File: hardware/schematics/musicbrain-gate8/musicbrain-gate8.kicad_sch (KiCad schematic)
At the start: 15 parts, among them J1 BUS, J2 GATES OUT, U1 74HCT595, U2 AMS1117-5.0

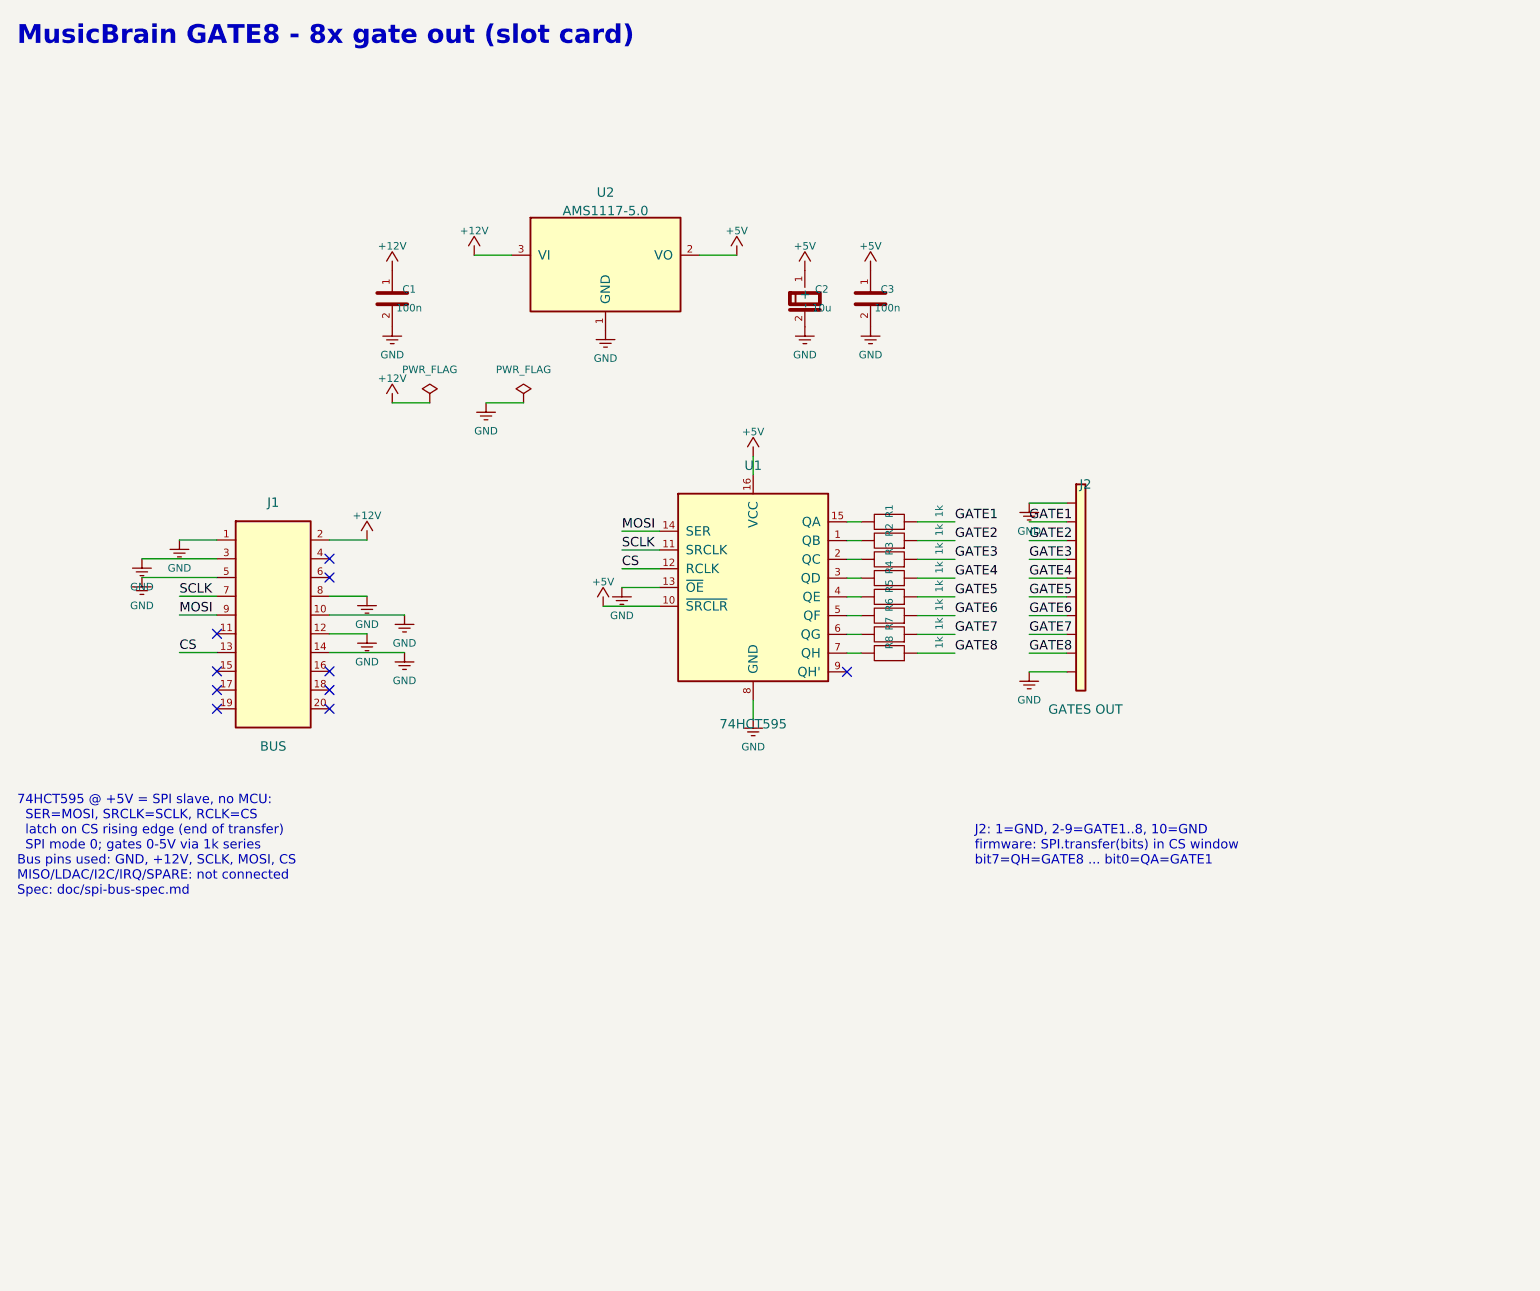
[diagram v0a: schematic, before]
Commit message: gate8 gen 2: 80x45, slot 2x12, freerouting; generator naar cardlib
- gen_gate.py (schlib+cardlib) vervangt gen_gate_sch.py + gen_gate_pcb_v11.py
  (gen 1, 35x80, eigen sexpr-bouwer van voor cardlib)
- J1 2x10 -> 2x12 via bus.j1_map; J2 1x10 gecentreerd, paneelinzet 4,04
- U1 74HCT595 rot 270: Q-uitgangen noord naar de 1k-kolommen, SPI/GND zuid
- AMS1117-5.0 + ontkoppeling in de oosthelft; +5V blijft lokaal
- prep_dsn.py: DSN-prep (GND-strip + randkrimp) nu een repo-script
- ERC 0, netcheck OK, DRC 0/0

Co-Authored-By: Claude Fable 5 <noreply@anthropic.com>
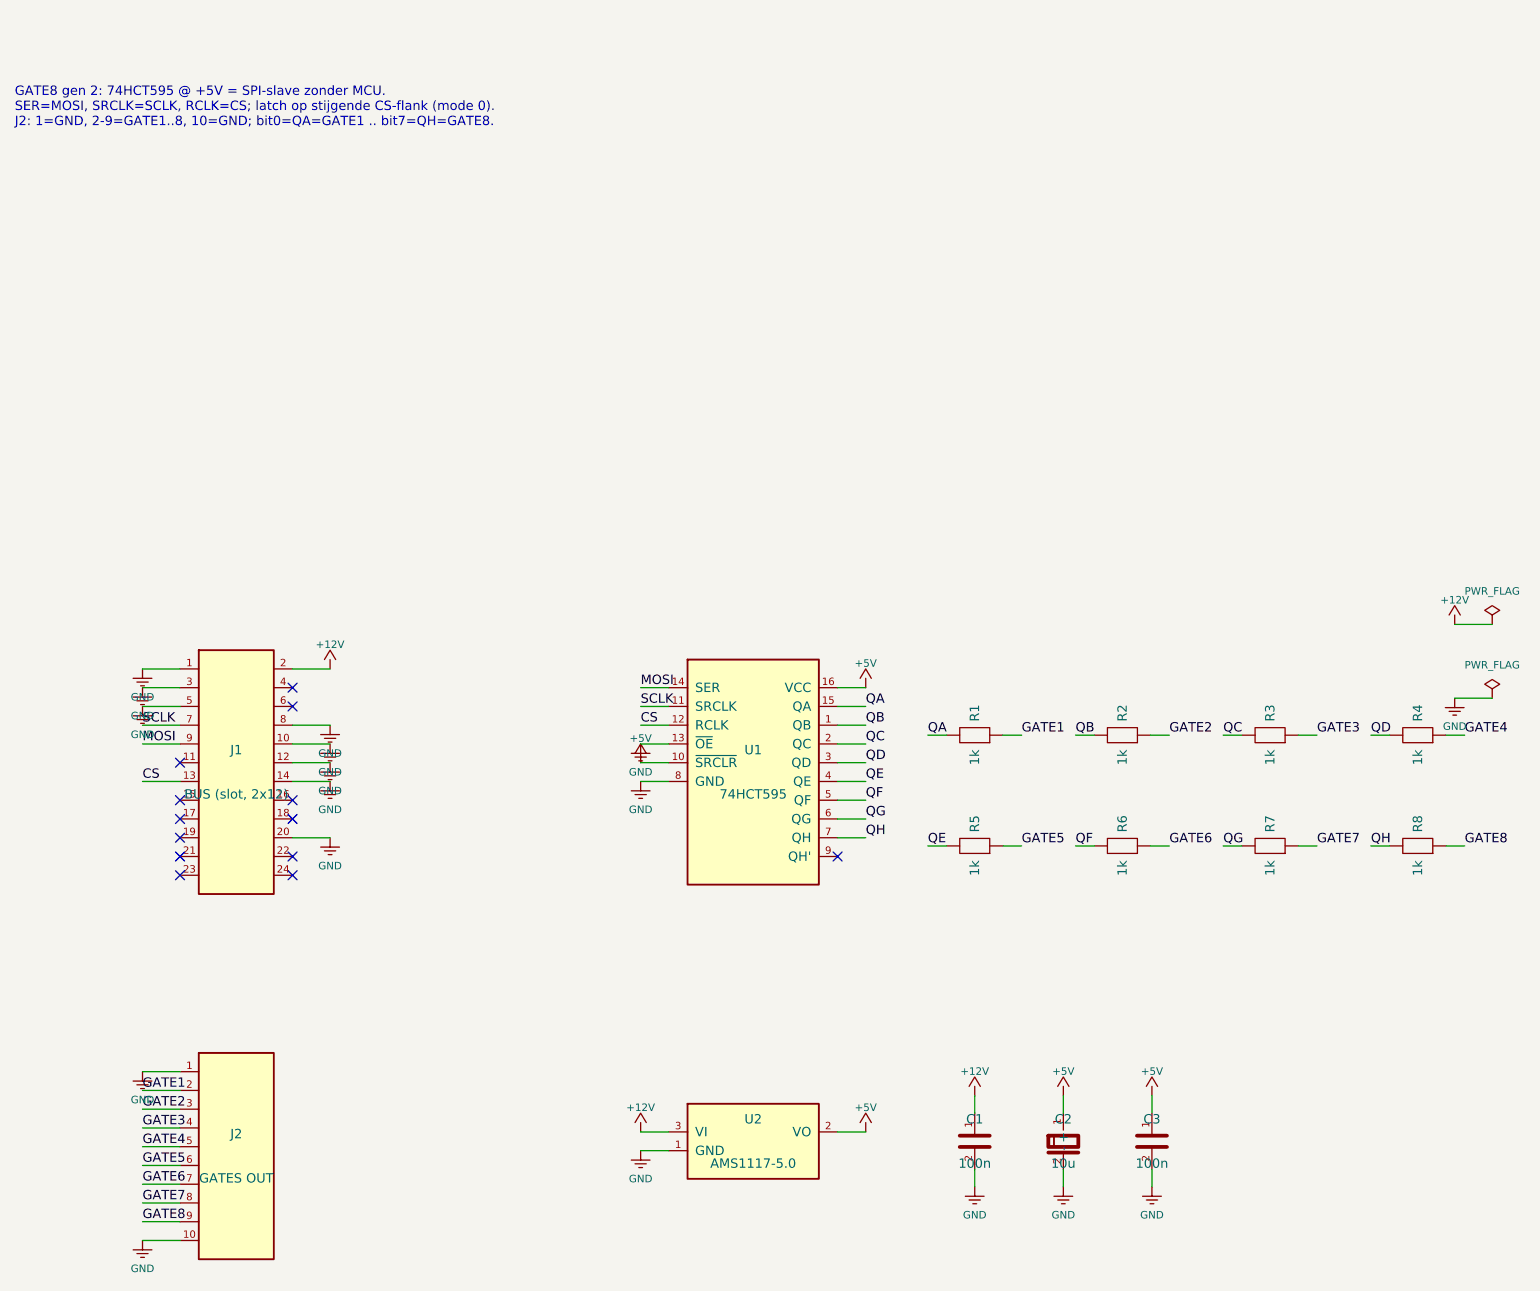
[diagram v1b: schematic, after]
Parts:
- removed J1: BUS, Connector_PinHeader_2.54mm:PinHeader_2x10_P2.54mm_Horizontal, symbol Custom:Conn_02x10
- added J1: BUS (slot, 2x12), Connector_PinHeader_2.54mm:PinHeader_2x12_P2.54mm_Horizontal, symbol Custom:Conn_02x12
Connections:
- net +12V: now also J1.2 (Pin_2)
- net CS: now also J1.13 (Pin_13)
- net GND: now also J1.1 (Pin_1), J1.10 (Pin_10), J1.12 (Pin_12), J1.14 (Pin_14), J1.20 (Pin_20), J1.3 (Pin_3), J1.5 (Pin_5), J1.8 (Pin_8)
- net MOSI: now also J1.9 (Pin_9)
- net SCLK: now also J1.7 (Pin_7)
- net QB: now reaches R2.1, U1.1 (QB)
- net QA: now reaches R1.1, U1.15 (QA)
- net QC: now reaches R3.1, U1.2 (QC)
- net QD: now reaches R4.1, U1.3 (QD)
- net QE: now reaches R5.1, U1.4 (QE)
- net QF: now reaches R6.1, U1.5 (QF)
- net QG: now reaches R7.1, U1.6 (QG)
- net QH: now reaches R8.1, U1.7 (QH)
- no-connect marks 10 -> 13
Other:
- note added: "GATE8 gen 2: 74HCT595 @ +5V = SPI-slave zonder MCU. SER=MOSI, SRCLK=SCLK, RCLK=CS; latch op stijgende CS-flank (mode 0). J2: 1=GND, 2-9=GATE1..8, 10=GND; bit0=QA=GATE1 .. bit7=QH=GATE8."
- note removed: "74HCT595 @ +5V = SPI slave, no MCU: SER=MOSI, SRCLK=SCLK, RCLK=CS latch on CS rising edge (end of transfer) SPI mode 0; gates 0-5V via 1k series Bus pins used: GND, +12V, SCLK, MOSI, CS MISO/LDAC/I2C/IRQ/SPARE: not connected Spec: doc/spi-bus-spec.md"
- note removed: "J2: 1=GND, 2-9=GATE1..8, 10=GND firmware: SPI.transfer(bits) in CS window bit7=QH=GATE8 ... bit0=QA=GATE1"
- note removed: "MusicBrain GATE8 - 8x gate out (slot card)"
